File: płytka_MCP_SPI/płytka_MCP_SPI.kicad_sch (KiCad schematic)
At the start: 29 parts, among them J1 A0, J10 V0, J11 Ext, J13 U2, J15 U2, J16 U3, J17 RS, J18 K, J19 A, J2 A1, J20 VDD, J21 GND, J23 VSS, J24 Conn_01x16_Pin, J25 LCD, J26 VCC, J27 SPI, J3 A2, J6 INTA, J7 INTB, J8 INTA, J9 RESET, U1 MCP23S17_SP

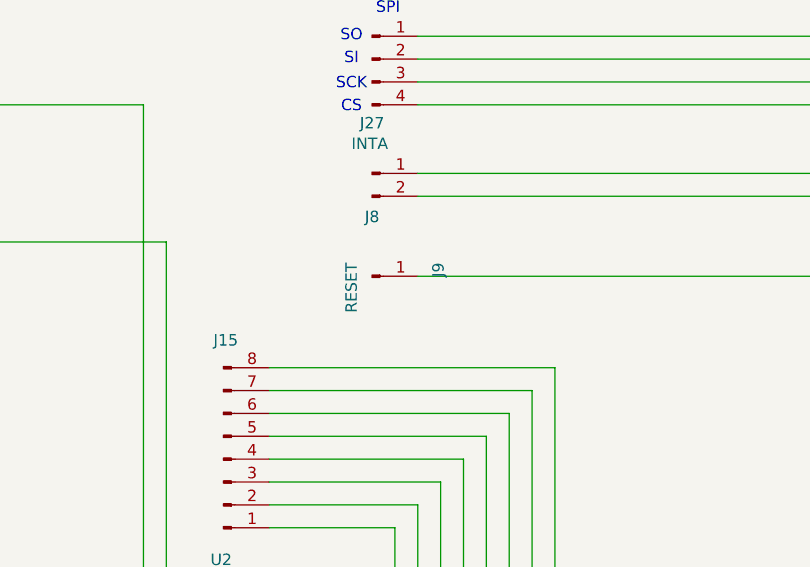
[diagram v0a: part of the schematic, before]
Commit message: Korekcja rozmiaru płytki, utworzenie draftow, do druku
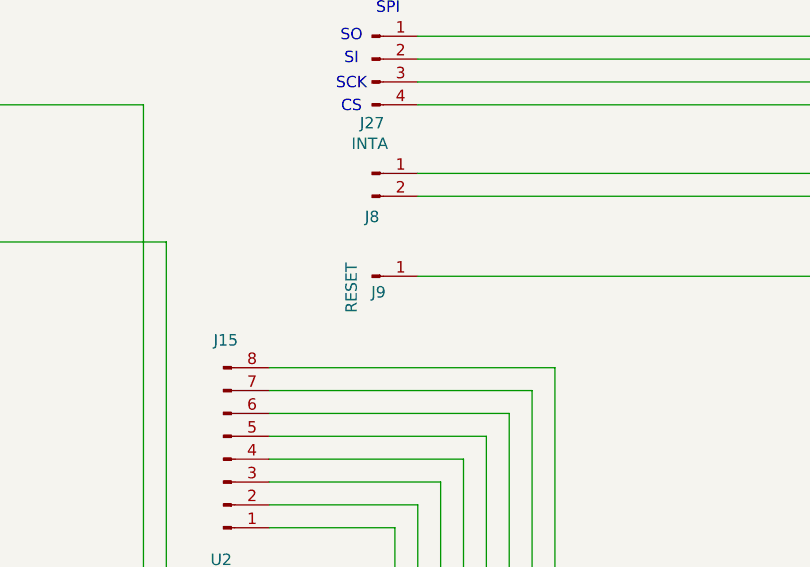
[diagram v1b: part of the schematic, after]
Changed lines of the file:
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@@
 		(dnp no)
 		(property "Reference" "J9"
-			(at 139.446 45.466 90)
+			(at 133.604 48.768 0)
 			(effects
 				(font
